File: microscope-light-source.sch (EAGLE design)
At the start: 17 parts, among them IC1 AVR-ATTINY13-DIP8, IC2 LM317, IC3 7805, J1 LED, J2 POT, J3 SINE, J4 SPARES, T1 2N7000

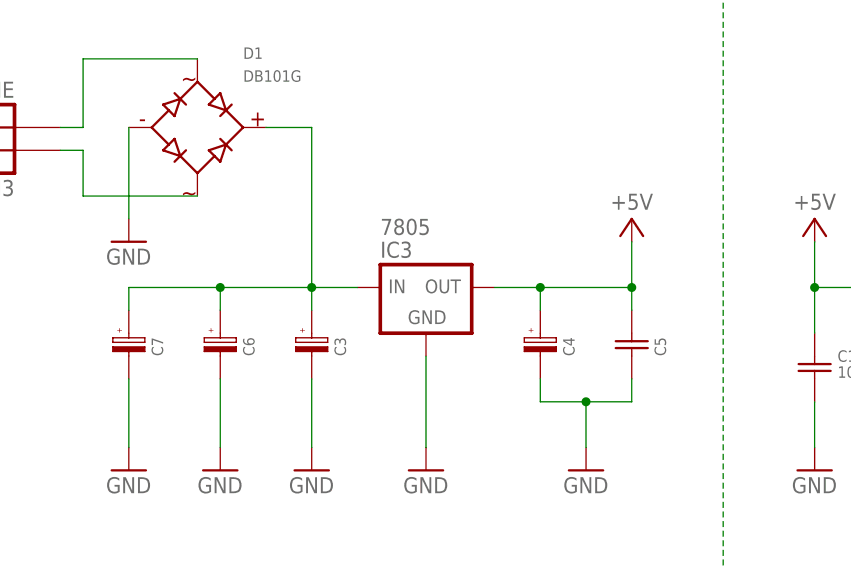
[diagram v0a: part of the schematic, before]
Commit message: C values, board re-jig
Values added for capacitors.
Voltage regulator rotated 180 deg to simplify trace routing.
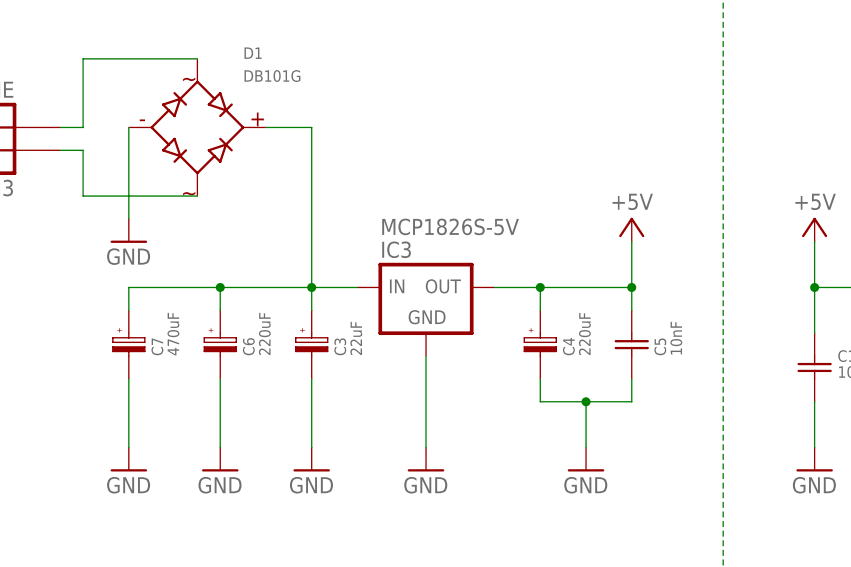
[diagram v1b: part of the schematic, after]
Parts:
- C3: value (none) -> 22uF
- C4, C6: value (none) -> 220uF
- C5: value (none) -> 10nF
- C7: value (none) -> 470uF
- IC3: value 7805 -> MCP1826S-5V
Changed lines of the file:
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@@
 <setting verticaltext="up"/>
 </settings>
-<grid distance="0.025" unitdist="inch" unit="inch" style="lines" multiple="1" display="yes" altdistance="0.01" altunitdist="inch" altunit="inch"/>
+<grid distance="0.1" unitdist="inch" unit="inch" style="lines" multiple="1" display="no" altdistance="0.01" altunitdist="inch" altunit="inch"/>
 <layers>
 <layer number="1" name="Top" color="4" fill="1" visible="no" active="no"/>
@@
 <part name="GND5" library="supply1" deviceset="GND" device=""/>
 <part name="P+4" library="supply1" deviceset="+5V" device=""/>
-<part name="IC3" library="tidyeagle" deviceset="VREG-3PIN" device="-IGO-TO220-HORZ-DRILL" value="7805"/>
-<part name="C3" library="tidyeagle" deviceset="CAPACITOR-POLARISED" device="-TH-5MM"/>
-<part name="C4" library="tidyeagle" deviceset="CAPACITOR-POLARISED" device="-TH-5MM"/>
-<part name="C5" library="tidyeagle" deviceset="CAPACITOR" device="-TH-5MM"/>
+<part name="IC3" library="tidyeagle" deviceset="VREG-3PIN" device="-IGO-TO220-HORZ-DRILL" value="MCP1826S-5V"/>
+<part name="C3" library="tidyeagle" deviceset="CAPACITOR-POLARISED" device="-TH-5MM" value="22uF"/>
+<part name="C4" library="tidyeagle" deviceset="CAPACITOR-POLARISED" device="-TH-5MM" value="220uF"/>
+<part name="C5" library="tidyeagle" deviceset="CAPACITOR" device="-TH-5MM" value="10nF"/>
 <part name="GND6" library="supply1" deviceset="GND" device=""/>
 <part name="GND7" library="supply1" deviceset="GND" device=""/>
@@
 <part name="J3" library="tidyeagle" deviceset="J02" device="-LONG" value="SINE"/>
 <part name="GND9" library="supply1" deviceset="GND" device=""/>
-<part name="C6" library="tidyeagle" deviceset="CAPACITOR-POLARISED" device="-TH-5MM"/>
+<part name="C6" library="tidyeagle" deviceset="CAPACITOR-POLARISED" device="-TH-5MM" value="220uF"/>
 <part name="GND10" library="supply1" deviceset="GND" device=""/>
-<part name="C7" library="tidyeagle" deviceset="CAPACITOR-POLARISED" device="-TH-10MM"/>
+<part name="C7" library="tidyeagle" deviceset="CAPACITOR-POLARISED" device="-TH-10MM" value="470uF"/>
 <part name="GND4" library="supply1" deviceset="GND" device=""/>
 <part name="P+3" library="supply1" deviceset="+5V" device=""/>
